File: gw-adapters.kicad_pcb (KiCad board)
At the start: 2 copper layers, 41.9 x 71.1 mm, 3 parts, among them J1 Floppy_Header, J2 TE 174552-1, J3 Floppy_DB25

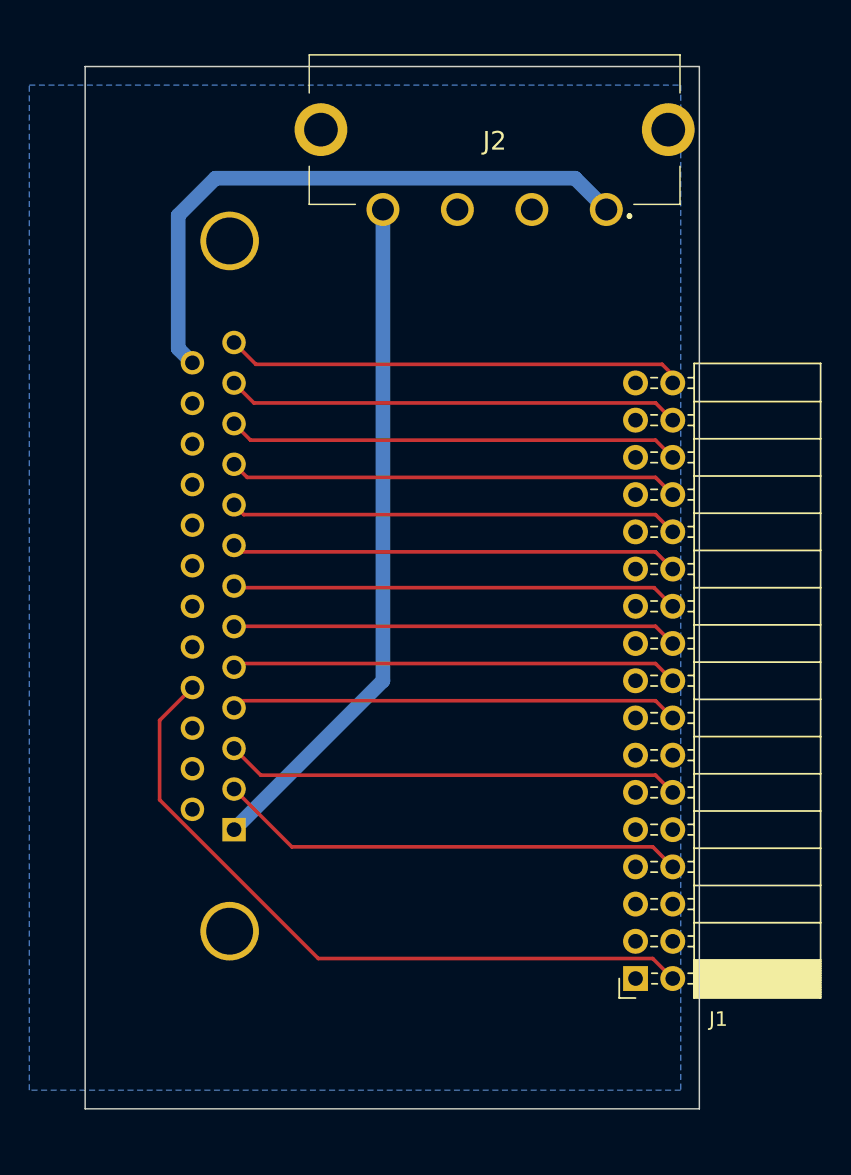
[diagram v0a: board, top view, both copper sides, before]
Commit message: Rerouted
Rerouted traces to allow for all components to be placed on the top of the board.
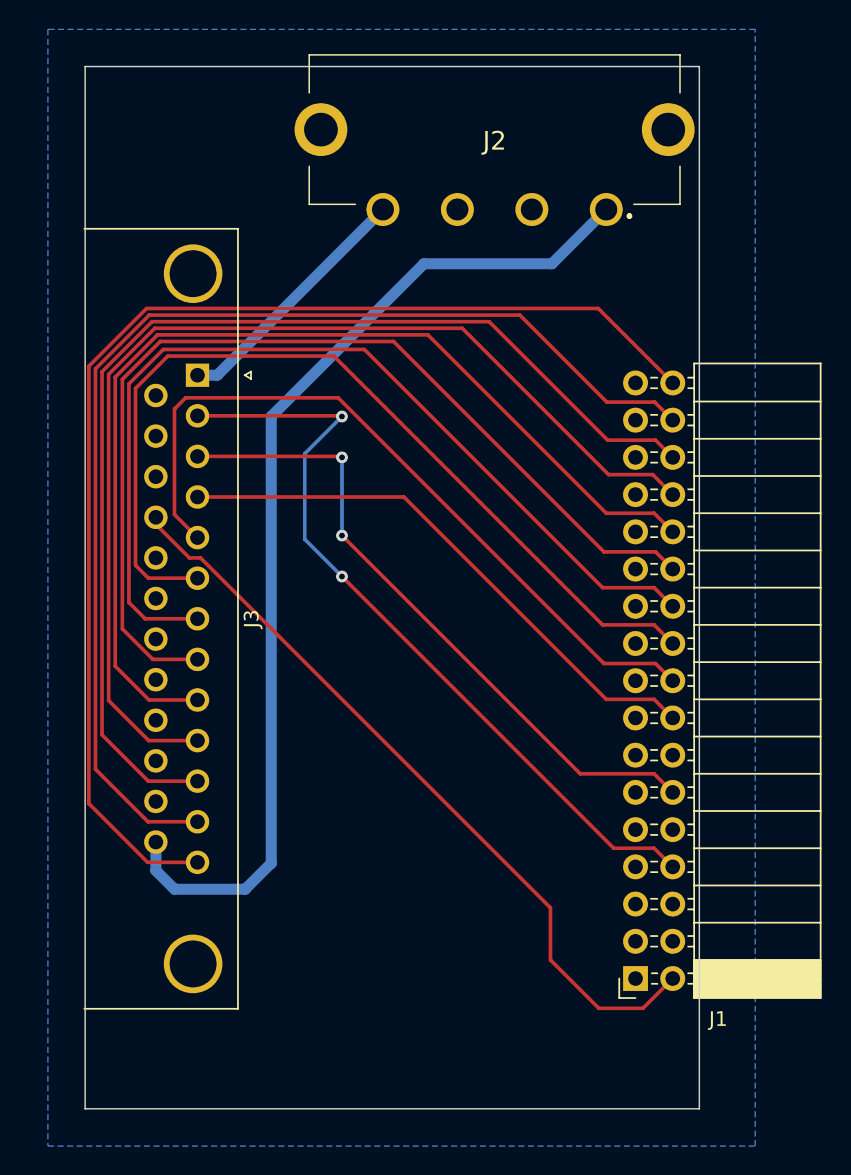
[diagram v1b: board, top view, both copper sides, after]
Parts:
- J3: moved to F.Cu
- moved J3 31.1 mm to (129.6, 76.9), turned to -90 degrees
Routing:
- net /Disk Change: track 31.4 -> 83.0 mm
- net /Head Select: track 31.0 -> 79.6 mm
- net /Read Data: track 30.9 -> 76.8 mm
- net /Write Protect: track 30.8 -> 73.9 mm
- net /Track 0: track 30.7 -> 71.1 mm
- net /Write Gate: track 30.6 -> 68.1 mm
- net /Write Data: track 30.5 -> 66.0 mm
- net /Step: track 30.4 -> 62.4 mm
- net +5V: track 46.5 -> 17.3 mm
- net +12V: track 41.6 -> 70.3 mm
- net /Index: track 32.1 -> 53.7 mm, vias 0 -> 2
- net /Direction: track 30.5 -> 51.7 mm
- net /Drive Select 1: track 31.2 -> 45.1 mm, vias 0 -> 2
- net /Motor 1: track 30.6 -> 38.7 mm
- net /Density Select: track 48.7 -> 53.0 mm
